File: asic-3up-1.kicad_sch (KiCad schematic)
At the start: 79 parts, among them J14 Conn_01x01, J15 Conn_01x01, J5 Conn_01x01, J7 Conn_01x01, U48 MCP1824T-1202E/OT, U49 MCP1824T-1202E/OT, U50 MCP1824T-1202E/OT, U51 MCP1824T-0802E, U52 MCP1824T-0802E, U53 MCP1824T-0802E, U54 BM1362AC_MODE1, U55 BM1362AC_MODE0, U56 BM1362AC_MODE1

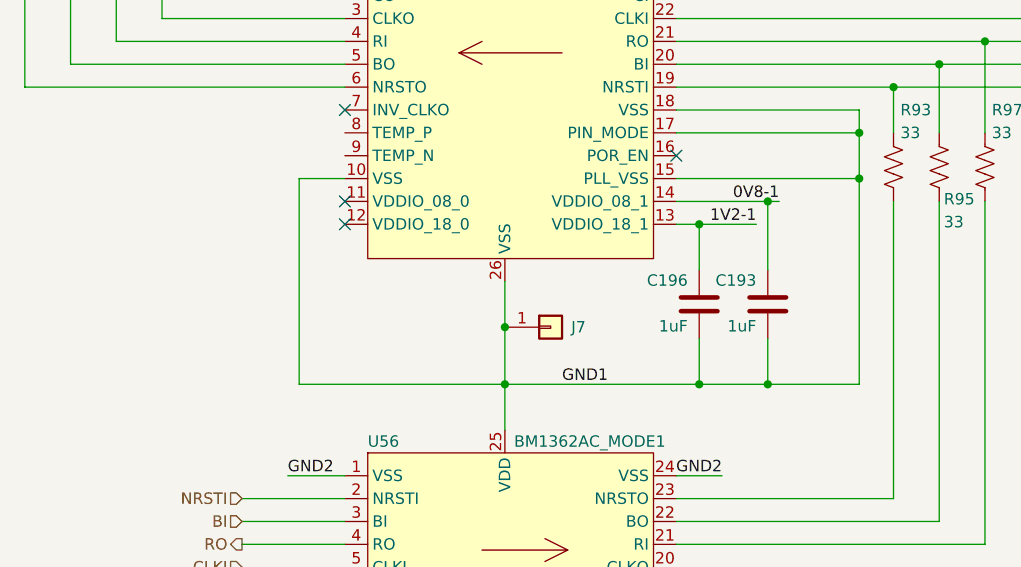
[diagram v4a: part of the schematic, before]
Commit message: added the heatsink mounting holes
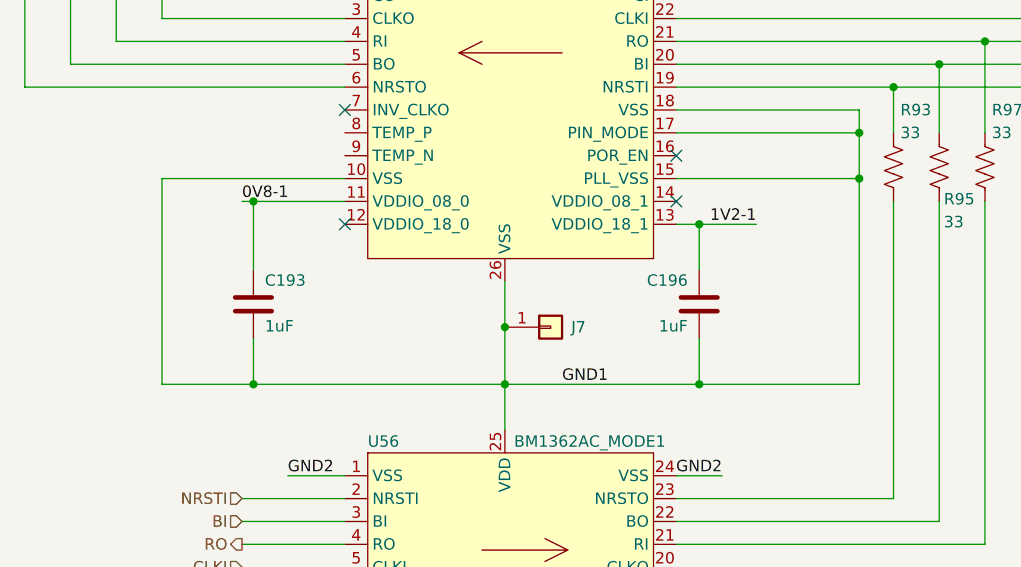
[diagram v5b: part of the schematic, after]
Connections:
- net 0V8-1: now also U55.11 (VDDIO_08_0); no longer U55.14 (VDDIO_08_1)
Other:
- moved on the sheet: C193
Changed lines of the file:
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@@
 	)
 	(junction
-		(at 278.13 139.7)
-		(diameter 0)
-		(color 0 0 0 0)
-	)
-	(junction
 		(at 124.46 181.61)
 		(diameter 0)
@@
 	)
 	(junction
-		(at 278.13 160.02)
-		(diameter 0)
-		(color 0 0 0 0)
-	)
-	(junction
 		(at 148.59 195.58)
 		(diameter 0.9144)
@@
 	)
 	(junction
+		(at 220.98 139.7)
+		(diameter 0)
+		(color 0 0 0 0)
+	)
+	(junction
 		(at 215.9 71.12)
 		(diameter 0)
@@
 	)
 	(junction
+		(at 220.98 160.02)
+		(diameter 0)
+		(color 0 0 0 0)
+	)
+	(junction
 		(at 205.74 66.04)
 		(diameter 0)
@@
 	)
 	(no_connect
-		(at 231.14 139.7)
+		(at 267.97 139.7)
 	)
 	(no_connect
@@
 	(wire
 		(pts
+			(xy 220.98 154.94) (xy 220.98 160.02)
+		)
+		(stroke
+			(width 0)
+			(type default)
+		)
+	)
+	(wire
+		(pts
 			(xy 91.44 181.61) (xy 91.44 184.15)
 		)
@@
 	(wire
 		(pts
-			(xy 278.13 160.02) (xy 288.29 160.02)
-		)
-		(stroke
-			(width 0)
-			(type default)
-		)
-	)
-	(wire
-		(pts
 			(xy 320.04 60.96) (xy 318.77 60.96)
 		)
@@
 	(wire
 		(pts
+			(xy 220.98 160.02) (xy 248.92 160.02)
+		)
+		(stroke
+			(width 0)
+			(type default)
+		)
+	)
+	(wire
+		(pts
 			(xy 248.92 104.14) (xy 248.92 109.22)
 		)
@@
 	(wire
 		(pts
-			(xy 231.14 137.16) (xy 226.06 137.16)
+			(xy 231.14 137.16) (xy 210.82 137.16)
 		)
 		(stroke
@@
 	(wire
 		(pts
-			(xy 270.51 160.02) (xy 278.13 160.02)
+			(xy 270.51 160.02) (xy 288.29 160.02)
 		)
 		(stroke
@@
 	(wire
 		(pts
-			(xy 278.13 139.7) (xy 267.97 139.7)
+			(xy 220.98 139.7) (xy 231.14 139.7)
 		)
 		(stroke
@@
 	(wire
 		(pts
-			(xy 278.13 139.7) (xy 278.13 147.32)
+			(xy 220.98 139.7) (xy 220.98 147.32)
 		)
 		(stroke
@@
 	(wire
 		(pts
+			(xy 210.82 160.02) (xy 220.98 160.02)
+		)
+		(stroke
+			(width 0)
+			(type default)
+		)
+	)
+	(wire
+		(pts
 			(xy 278.13 104.14) (xy 270.51 104.14)
 		)
@@
 	(wire
 		(pts
-			(xy 278.13 154.94) (xy 278.13 160.02)
-		)
-		(stroke
-			(width 0)
-			(type default)
-		)
-	)
-	(wire
-		(pts
 			(xy 356.87 128.27) (xy 346.71 128.27)
 		)
@@
 	(wire
 		(pts
-			(xy 226.06 160.02) (xy 248.92 160.02)
-		)
-		(stroke
-			(width 0)
-			(type default)
-		)
-	)
-	(wire
-		(pts
 			(xy 210.82 83.82) (xy 210.82 119.38)
 		)
@@
 	(wire
 		(pts
-			(xy 226.06 137.16) (xy 226.06 160.02)
+			(xy 210.82 137.16) (xy 210.82 160.02)
 		)
 		(stroke
@@
 	(wire
 		(pts
-			(xy 279.4 139.7) (xy 278.13 139.7)
+			(xy 220.98 139.7) (xy 219.71 139.7)
 		)
 		(stroke
@@
 	)
 	(label "0V8-1"
-		(at 279.4 139.7 180)
+		(at 219.71 139.7 0)
 		(fields_autoplaced yes)
 		(effects
@@
 				(size 1.27 1.27)
 			)
-			(justify right bottom)
+			(justify left bottom)
 		)
 	)
@@
 	(symbol
 		(lib_id "Device:C")
-		(at 278.13 151.13 0)
-		(mirror y)
+		(at 220.98 151.13 0)
 		(unit 1)
 		(exclude_from_sim no)
@@
 		(dnp no)
 		(property "Reference" "C193"
-			(at 276.86 149.225 0)
+			(at 222.25 149.225 0)
 			(effects
 				(font
@@
 		)
 		(property "Value" "1uF"
-			(at 276.86 154.305 0)
+			(at 222.25 154.305 0)
 			(effects
 				(font
@@
 		)
 		(property "Footprint" "Capacitor_SMD:C_0402_1005Metric"
-			(at 278.13 151.13 0)
+			(at 220.98 151.13 0)
 			(effects
 				(font
@@
 		)
 		(property "Datasheet" ""
-			(at 278.13 151.13 0)
+			(at 220.98 151.13 0)
 			(effects
 				(font
@@
 		)
 		(property "Description" ""
-			(at 278.13 151.13 0)
+			(at 220.98 151.13 0)
 			(effects
 				(font
@@
 		)
 		(property "DK" "587-5514-1-ND"
-			(at 278.13 151.13 0)
+			(at 220.98 151.13 0)
 			(effects
 				(font
@@
 		)
 		(property "PARTNO" "EMK105BJ105MV-F"
-			(at 278.13 151.13 0)
+			(at 220.98 151.13 0)
 			(effects
 				(font

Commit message: placements done. shrunk test points
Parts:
- TP100, TP101, TP102, TP103, TP104, TP105, TP106, TP107, TP108, TP109, TP110, TP111, TP112, TP113, TP114, TP115, TP116, TP117, TP118, TP119, TP120: footprint TestPoint:TestPoint_Pad_D1.5mm -> TestPoint:TestPoint_Pad_D1.0mm
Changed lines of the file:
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@@
 			)
 		)
-		(property "Footprint" "TestPoint:TestPoint_Pad_D1.5mm"
+		(property "Footprint" "TestPoint:TestPoint_Pad_D1.0mm"
 			(at 160.02 176.53 0)
 			(effects
@@
 			)
 		)
-		(property "Footprint" "TestPoint:TestPoint_Pad_D1.5mm"
+		(property "Footprint" "TestPoint:TestPoint_Pad_D1.0mm"
 			(at 160.02 119.38 0)
 			(effects
@@
 			)
 		)
-		(property "Footprint" "TestPoint:TestPoint_Pad_D1.5mm"
+		(property "Footprint" "TestPoint:TestPoint_Pad_D1.0mm"
 			(at 318.77 121.92 0)
 			(effects
@@
 			)
 		)
-		(property "Footprint" "TestPoint:TestPoint_Pad_D1.5mm"
+		(property "Footprint" "TestPoint:TestPoint_Pad_D1.0mm"
 			(at 186.69 66.04 0)
 			(effects
@@
 			)
 		)
-		(property "Footprint" "TestPoint:TestPoint_Pad_D1.5mm"
+		(property "Footprint" "TestPoint:TestPoint_Pad_D1.0mm"
 			(at 318.77 132.08 0)
 			(effects
@@
 			)
 		)
-		(property "Footprint" "TestPoint:TestPoint_Pad_D1.5mm"
+		(property "Footprint" "TestPoint:TestPoint_Pad_D1.0mm"
 			(at 320.04 66.04 0)
 			(effects
@@
 			)
 		)
-		(property "Footprint" "TestPoint:TestPoint_Pad_D1.5mm"
+		(property "Footprint" "TestPoint:TestPoint_Pad_D1.0mm"
 			(at 318.77 124.46 0)
 			(effects
@@
 			)
 		)
-		(property "Footprint" "TestPoint:TestPoint_Pad_D1.5mm"
+		(property "Footprint" "TestPoint:TestPoint_Pad_D1.0mm"
 			(at 318.77 127 0)
 			(effects
@@
 			)
 		)
-		(property "Footprint" "TestPoint:TestPoint_Pad_D1.5mm"
+		(property "Footprint" "TestPoint:TestPoint_Pad_D1.0mm"
 			(at 320.04 71.12 0)
 			(effects
@@
 			)
 		)
-		(property "Footprint" "TestPoint:TestPoint_Pad_D1.5mm"
+		(property "Footprint" "TestPoint:TestPoint_Pad_D1.0mm"
 			(at 320.04 73.66 0)
 			(effects
@@
 			)
 		)
-		(property "Footprint" "TestPoint:TestPoint_Pad_D1.5mm"
+		(property "Footprint" "TestPoint:TestPoint_Pad_D1.0mm"
 			(at 100.33 119.38 0)
 			(effects
@@
 			)
 		)
-		(property "Footprint" "TestPoint:TestPoint_Pad_D1.5mm"
+		(property "Footprint" "TestPoint:TestPoint_Pad_D1.0mm"
 			(at 320.04 68.58 0)
 			(effects
@@
 			)
 		)
-		(property "Footprint" "TestPoint:TestPoint_Pad_D1.5mm"
+		(property "Footprint" "TestPoint:TestPoint_Pad_D1.0mm"
 			(at 318.77 129.54 0)
 			(effects
@@
 			)
 		)
-		(property "Footprint" "TestPoint:TestPoint_Pad_D1.5mm"
+		(property "Footprint" "TestPoint:TestPoint_Pad_D1.0mm"
 			(at 100.33 60.96 0)
 			(effects
@@
 			)
 		)
-		(property "Footprint" "TestPoint:TestPoint_Pad_D1.5mm"
+		(property "Footprint" "TestPoint:TestPoint_Pad_D1.0mm"
 			(at 320.04 76.2 0)
 			(effects
@@
 			)
 		)
-		(property "Footprint" "TestPoint:TestPoint_Pad_D1.5mm"
+		(property "Footprint" "TestPoint:TestPoint_Pad_D1.0mm"
 			(at 160.02 60.96 0)
 			(effects
@@
 			)
 		)
-		(property "Footprint" "TestPoint:TestPoint_Pad_D1.5mm"
+		(property "Footprint" "TestPoint:TestPoint_Pad_D1.0mm"
 			(at 100.33 176.53 0)
 			(effects
@@
 			)
 		)
-		(property "Footprint" "TestPoint:TestPoint_Pad_D1.5mm"
+		(property "Footprint" "TestPoint:TestPoint_Pad_D1.0mm"
 			(at 186.69 71.12 0)
 			(effects
@@
 			)
 		)
-		(property "Footprint" "TestPoint:TestPoint_Pad_D1.5mm"
+		(property "Footprint" "TestPoint:TestPoint_Pad_D1.0mm"
 			(at 186.69 68.58 0)
 			(effects
@@
 			)
 		)
-		(property "Footprint" "TestPoint:TestPoint_Pad_D1.5mm"
+		(property "Footprint" "TestPoint:TestPoint_Pad_D1.0mm"
 			(at 186.69 73.66 0)
 			(effects
@@
 			)
 		)
-		(property "Footprint" "TestPoint:TestPoint_Pad_D1.5mm"
+		(property "Footprint" "TestPoint:TestPoint_Pad_D1.0mm"
 			(at 186.69 76.2 0)
 			(effects

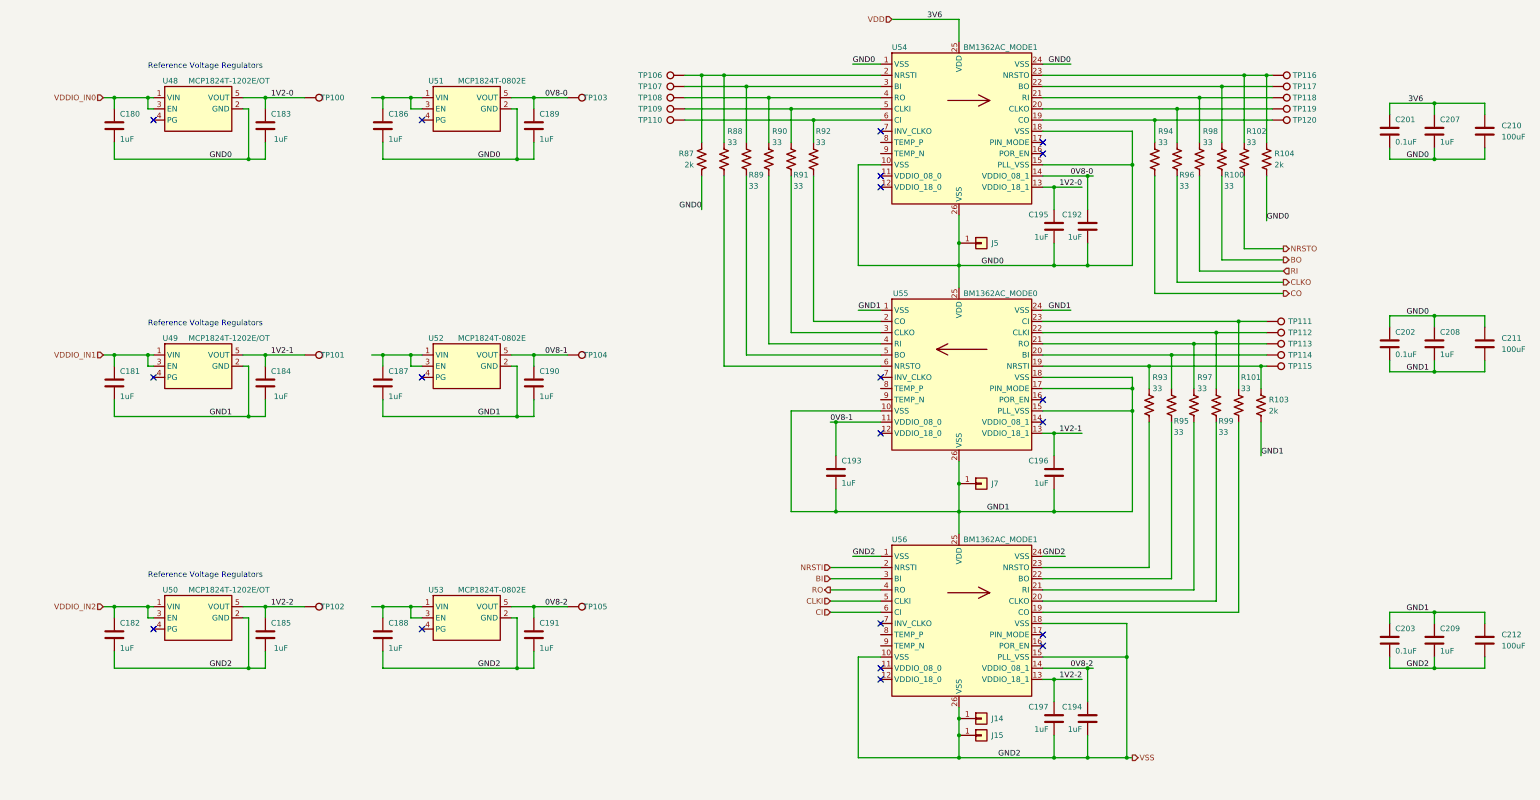
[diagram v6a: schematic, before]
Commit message: added temp sensors. wired up (hopeful) vreg EN circuit. lots of LDO routing.
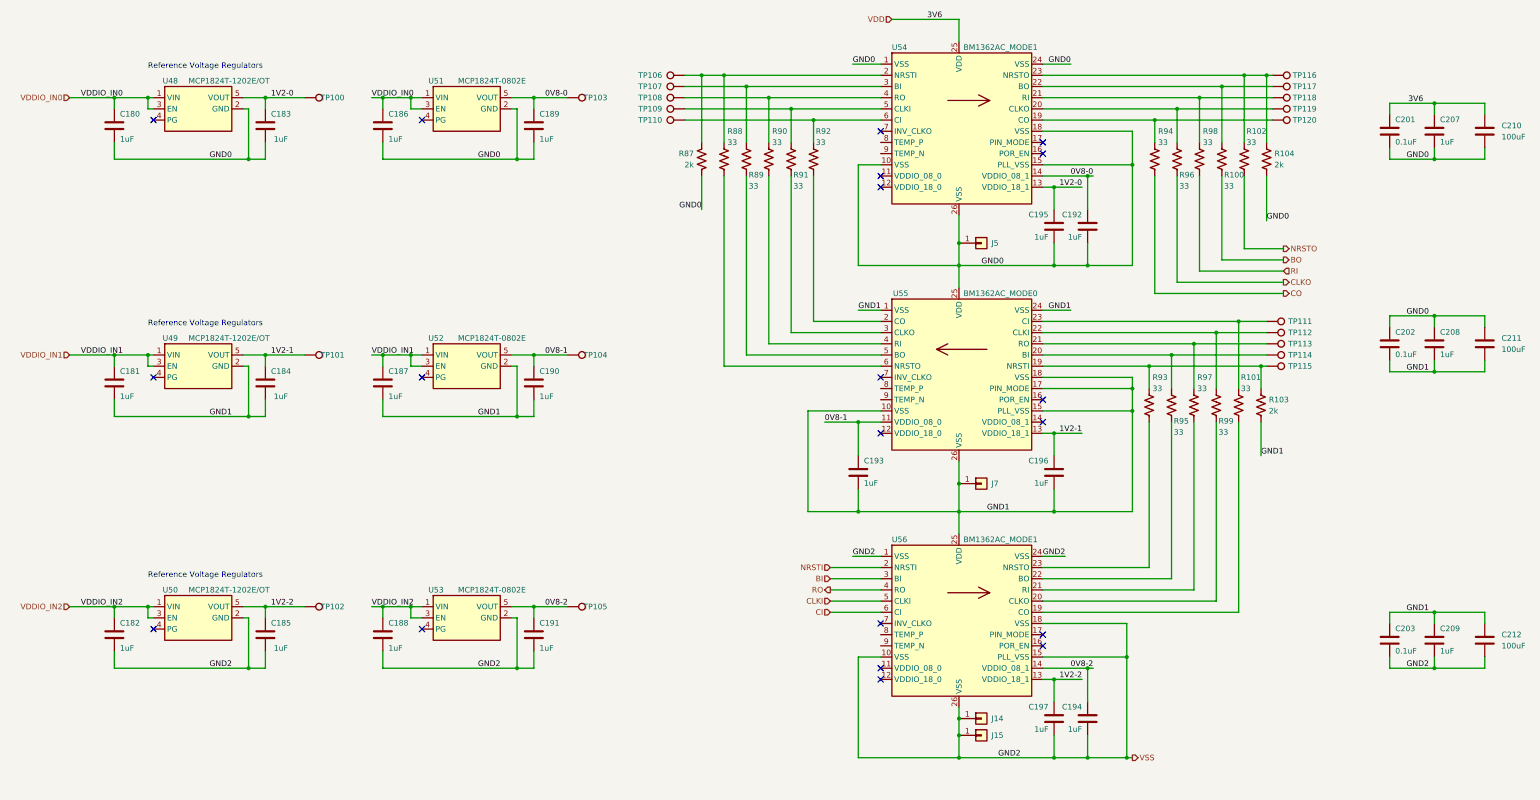
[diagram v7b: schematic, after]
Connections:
- net VDDIO_IN0: now also C186.1, U51.1 (VIN), U51.3 (EN)
- net VDDIO_IN1: now also C187.1, U52.1 (VIN), U52.3 (EN)
- net VDDIO_IN2: now also C188.1, U53.1 (VIN), U53.3 (EN)
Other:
- moved on the sheet: C193
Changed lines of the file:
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@@
 	)
 	(junction
-		(at 270.51 160.02)
-		(diameter 0)
-		(color 0 0 0 0)
-	)
-	(junction
 		(at 248.92 160.02)
 		(diameter 0)
@@
 	)
 	(junction
+		(at 226.06 139.7)
+		(diameter 0)
+		(color 0 0 0 0)
+	)
+	(junction
+		(at 270.51 160.02)
+		(diameter 0)
+		(color 0 0 0 0)
+	)
+	(junction
 		(at 91.44 124.46)
 		(diameter 0.9144)
@@
 	)
 	(junction
-		(at 220.98 139.7)
-		(diameter 0)
-		(color 0 0 0 0)
-	)
-	(junction
 		(at 215.9 71.12)
 		(diameter 0)
@@
 	)
 	(junction
+		(at 226.06 160.02)
+		(diameter 0)
+		(color 0 0 0 0)
+	)
+	(junction
 		(at 152.4 181.61)
 		(diameter 0.9144)
@@
 	)
 	(junction
-		(at 220.98 160.02)
-		(diameter 0)
-		(color 0 0 0 0)
-	)
-	(junction
 		(at 205.74 66.04)
 		(diameter 0)
@@
 	(wire
 		(pts
-			(xy 220.98 154.94) (xy 220.98 160.02)
+			(xy 226.06 154.94) (xy 226.06 160.02)
 		)
 		(stroke
@@
 	(wire
 		(pts
-			(xy 220.98 160.02) (xy 248.92 160.02)
-		)
-		(stroke
-			(width 0)
-			(type default)
-		)
-	)
-	(wire
-		(pts
 			(xy 248.92 104.14) (xy 248.92 109.22)
 		)
@@
 	(wire
 		(pts
-			(xy 231.14 137.16) (xy 210.82 137.16)
+			(xy 231.14 137.16) (xy 214.63 137.16)
 		)
 		(stroke
@@
 	(wire
 		(pts
-			(xy 270.51 160.02) (xy 288.29 160.02)
-		)
-		(stroke
-			(width 0)
-			(type default)
-		)
-	)
-	(wire
-		(pts
 			(xy 248.92 92.71) (xy 248.92 99.06)
 		)
@@
 	(wire
 		(pts
-			(xy 220.98 139.7) (xy 231.14 139.7)
-		)
-		(stroke
-			(width 0)
-			(type default)
-		)
-	)
-	(wire
-		(pts
-			(xy 220.98 139.7) (xy 220.98 147.32)
+			(xy 226.06 139.7) (xy 226.06 147.32)
 		)
 		(stroke
@@
 	(wire
 		(pts
-			(xy 210.82 160.02) (xy 220.98 160.02)
+			(xy 214.63 160.02) (xy 226.06 160.02)
 		)
 		(stroke
@@
 	(wire
 		(pts
+			(xy 270.51 160.02) (xy 288.29 160.02)
+		)
+		(stroke
+			(width 0)
+			(type default)
+		)
+	)
+	(wire
+		(pts
 			(xy 186.69 71.12) (xy 215.9 71.12)
 		)
@@
 	(wire
 		(pts
-			(xy 210.82 137.16) (xy 210.82 160.02)
+			(xy 214.63 137.16) (xy 214.63 160.02)
 		)
 		(stroke
@@
 	(wire
 		(pts
+			(xy 226.06 160.02) (xy 248.92 160.02)
+		)
+		(stroke
+			(width 0)
+			(type default)
+		)
+	)
+	(wire
+		(pts
 			(xy 87.63 68.58) (xy 87.63 80.01)
 		)
@@
 	(wire
 		(pts
+			(xy 226.06 139.7) (xy 231.14 139.7)
+		)
+		(stroke
+			(width 0)
+			(type default)
+		)
+	)
+	(wire
+		(pts
 			(xy 64.77 68.58) (xy 66.04 68.58)
 		)
@@
 	(wire
 		(pts
-			(xy 54.61 124.46) (xy 57.15 124.46)
+			(xy 46.99 124.46) (xy 57.15 124.46)
 		)
 		(stroke
@@
 	(wire
 		(pts
-			(xy 54.61 66.04) (xy 57.15 66.04)
+			(xy 46.99 66.04) (xy 57.15 66.04)
 		)
 		(stroke
@@
 	(wire
 		(pts
-			(xy 54.61 181.61) (xy 57.15 181.61)
+			(xy 46.99 181.61) (xy 57.15 181.61)
 		)
 		(stroke
@@
 	(wire
 		(pts
-			(xy 220.98 139.7) (xy 219.71 139.7)
+			(xy 218.44 139.7) (xy 226.06 139.7)
 		)
 		(stroke
@@
 		)
 	)
+	(label "VDDIO_IN2"
+		(at 115.57 181.61 0)
+		(fields_autoplaced yes)
+		(effects
+			(font
+				(size 1.27 1.27)
+			)
+			(justify left bottom)
+		)
+	)
 	(label "1V2-2"
 		(at 276.86 198.12 180)
@@
 		)
 	)
+	(label "VDDIO_IN0"
+		(at 49.53 66.04 0)
+		(fields_autoplaced yes)
+		(effects
+			(font
+				(size 1.27 1.27)
+			)
+			(justify left bottom)
+		)
+	)
 	(label "GND0"
 		(at 350.52 80.01 0)
@@
 		)
 	)
+	(label "VDDIO_IN2"
+		(at 49.53 181.61 0)
+		(fields_autoplaced yes)
+		(effects
+			(font
+				(size 1.27 1.27)
+			)
+			(justify left bottom)
+		)
+	)
 	(label "GND2"
 		(at 224.79 170.18 0)
@@
 	)
 	(label "0V8-1"
-		(at 219.71 139.7 0)
+		(at 218.44 139.7 0)
 		(fields_autoplaced yes)
 		(effects
@@
 		)
 	)
+	(label "VDDIO_IN1"
+		(at 115.57 124.46 0)
+		(fields_autoplaced yes)
+		(effects
+			(font
+				(size 1.27 1.27)
+			)
+			(justify left bottom)
+		)
+	)
 	(label "0V8-2"
 		(at 279.4 195.58 180)
@@
 		)
 	)
+	(label "VDDIO_IN0"
+		(at 115.57 66.04 0)
+		(fields_autoplaced yes)
+		(effects
+			(font
+				(size 1.27 1.27)
+			)
+			(justify left bottom)
+		)
+	)
 	(label "GND2"
 		(at 257.81 215.9 0)
@@
 		)
 	)
+	(label "VDDIO_IN1"
+		(at 49.53 124.46 0)
+		(fields_autoplaced yes)
+		(effects
+			(font
+				(size 1.27 1.27)
+			)
+			(justify left bottom)
+		)
+	)
 	(label "GND1"
 		(at 226.06 114.3 0)
@@
 	(hierarchical_label "VDDIO_IN0"
 		(shape input)
-		(at 54.61 66.04 180)
+		(at 46.99 66.04 180)
 		(fields_autoplaced yes)
 		(effects
@@
 	(hierarchical_label "VDDIO_IN1"
 		(shape input)
-		(at 54.61 124.46 180)
+		(at 46.99 124.46 180)
 		(fields_autoplaced yes)
 		(effects
@@
 	(hierarchical_label "VDDIO_IN2"
 		(shape input)
-		(at 54.61 181.61 180)
+		(at 46.99 181.61 180)
 		(fields_autoplaced yes)
 		(effects
@@
 	(symbol
 		(lib_id "Device:C")
-		(at 220.98 151.13 0)
+		(at 226.06 151.13 0)
 		(unit 1)
 		(exclude_from_sim no)
@@
 		(dnp no)
 		(property "Reference" "C193"
-			(at 222.25 149.225 0)
+			(at 227.33 149.225 0)
 			(effects
 				(font
@@
 		)
 		(property "Value" "1uF"
-			(at 222.25 154.305 0)
+			(at 227.33 154.305 0)
 			(effects
 				(font
@@
 		)
 		(property "Footprint" "Capacitor_SMD:C_0402_1005Metric"
-			(at 220.98 151.13 0)
+			(at 226.06 151.13 0)
 			(effects
 				(font
@@
 		)
 		(property "Datasheet" ""
-			(at 220.98 151.13 0)
+			(at 226.06 151.13 0)
 			(effects
 				(font
@@
 		)
 		(property "Description" ""
-			(at 220.98 151.13 0)
+			(at 226.06 151.13 0)
 			(effects
 				(font
@@
 		)
 		(property "DK" "587-5514-1-ND"
-			(at 220.98 151.13 0)
+			(at 226.06 151.13 0)
 			(effects
 				(font
@@
 		)
 		(property "PARTNO" "EMK105BJ105MV-F"
-			(at 220.98 151.13 0)
+			(at 226.06 151.13 0)
 			(effects
 				(font
